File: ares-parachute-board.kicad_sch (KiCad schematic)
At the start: 5 parts, among them J1 Conn_01x16_Female, J2 Conn_01x16_Female, J3 Conn_01x02_Male, U1 STM32F103CBTx

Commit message: rename project
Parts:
- added U2, U3: LIS2DH, Package_LGA:LGA-14_2x2mm_P0.35mm_LayoutBorder3x4y, symbol Sensor_Motion:LIS2DH
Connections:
- new net: U3.10 (GND), U3.11 (GND), U3.12 (GND), U3.13 (GND), U3.14 (GND), U3.9 (GND)
- new net: U2.10 (GND), U2.11 (GND), U2.12 (GND), U2.13 (GND), U2.14 (GND), U2.9 (GND)
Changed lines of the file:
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@@
+	)
+	(symbol
+		(lib_id "Sensor_Motion:LIS2DH")
+		(at 101.6 158.75 0)
+		(unit 1)
+		(exclude_from_sim no)
+		(in_bom yes)
+		(on_board yes)
+		(dnp no)
+		(fields_autoplaced yes)
+		(property "Reference" "U3"
+			(at 103.7941 171.45 0)
+			(effects
+				(font
+					(size 1.27 1.27)
+				)
+				(justify left)
+			)
+		)
+		(property "Value" "LIS2DH"
+			(at 103.7941 173.99 0)
+			(effects
+				(font
+					(size 1.27 1.27)
+				)
+				(justify left)
+			)
+		)
+		(property "Footprint" "Package_LGA:LGA-14_2x2mm_P0.35mm_LayoutBorder3x4y"
+			(at 101.6 170.18 0)
+			(effects
+				(font
+					(size 1.27 1.27)
+				)
+				(hide yes)
+			)
+		)
+		(property "Datasheet" "http://www.st.com/web/en/resource/technical/document/datasheet/DM00042751.pdf"
+			(at 101.6 173.99 0)
+			(effects
+				(font
+					(size 1.27 1.27)
+				)
+				(hide yes)
+			)
+		)
+		(property "Description" "3-Axis Accelerometer, 2/4/8/16g range, I2C/SPI interface, LGA-14"
+			(at 101.6 158.75 0)
+			(effects
+				(font
+					(size 1.27 1.27)
+				)
+				(hide yes)
+			)
+		)
+		(pin "3"
+		)
+		(pin "5"
+		)
+		(pin "12"
+		)
+		(pin "14"
+		)
+		(pin "2"
+		)
+		(pin "13"
+		)
+		(pin "6"
+		)
+		(pin "4"
+		)
+		(pin "11"
+		)
+		(pin "10"
+		)
+		(pin "1"
+		)
+		(pin "9"
+		)
+		(pin "8"
+		)
+		(pin "7"
+		)
+		(instances
+			(project "asyd-parachute"
+				(path "/690fc002-96ff-4ebc-bc23-96072f93f7f5"
+					(reference "U3")
+					(unit 1)
+				)
+			)
+		)
+	)
+	(symbol
+		(lib_id "Sensor_Motion:LIS2DH")
+		(at 71.12 158.75 0)
+		(unit 1)
+		(exclude_from_sim no)
+		(in_bom yes)
+		(on_board yes)
+		(dnp no)
+		(fields_autoplaced yes)
+		(property "Reference" "U2"
+			(at 73.3141 171.45 0)
+			(effects
+				(font
+					(size 1.27 1.27)
+				)
+				(justify left)
+			)
+		)
+		(property "Value" "LIS2DH"
+			(at 73.3141 173.99 0)
+			(effects
+				(font
+					(size 1.27 1.27)
+				)
+				(justify left)
+			)
+		)
+		(property "Footprint" "Package_LGA:LGA-14_2x2mm_P0.35mm_LayoutBorder3x4y"
+			(at 71.12 170.18 0)
+			(effects
+				(font
+					(size 1.27 1.27)
+				)
+				(hide yes)
+			)
+		)
+		(property "Datasheet" "http://www.st.com/web/en/resource/technical/document/datasheet/DM00042751.pdf"
+			(at 71.12 173.99 0)
+			(effects
+				(font
+					(size 1.27 1.27)
+				)
+				(hide yes)
+			)
+		)
+		(property "Description" "3-Axis Accelerometer, 2/4/8/16g range, I2C/SPI interface, LGA-14"
+			(at 71.12 158.75 0)
+			(effects
+				(font
+					(size 1.27 1.27)
+				)
+				(hide yes)
+			)
+		)
+		(pin "3"
+		)
+		(pin "5"
+		)
+		(pin "12"
+		)
+		(pin "14"
+		)
+		(pin "2"
+		)
+		(pin "13"
+		)
+		(pin "6"
+		)
+		(pin "4"
+		)
+		(pin "11"
+		)
+		(pin "10"
+		)
+		(pin "1"
+		)
+		(pin "9"
+		)
+		(pin "8"
+		)
+		(pin "7"
+		)
+		(instances
+			(project ""
+				(path "/690fc002-96ff-4ebc-bc23-96072f93f7f5"
+					(reference "U2")
+					(unit 1)
+				)
+			)
+		)
 	)
 	(symbol

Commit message: update, component selection almost done
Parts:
- removed U2, U3: LIS2DH, Package_LGA:LGA-14_2x2mm_P0.35mm_LayoutBorder3x4y, symbol Sensor_Motion:LIS2DH
- added C1, C2: 20p, Capacitor_SMD:C_0603_1608Metric, symbol Device:C
- added C3, C4: 12.5p, Capacitor_SMD:C_0603_1608Metric, symbol Device:C
- added C5, C6: 47p, Capacitor_SMD:C_0603_1608Metric, symbol Device:C
- added J4: MPT 0.5/2-2.54, TerminalBlock_Phoenix:TerminalBlock_Phoenix_MPT-0,5-2-2.54_1x02_P2.54mm_Horizontal, symbol Connector:Screw_Terminal_01x02
- added J5: Conn_ARM_JTAG_SWD_10, easyeda_exported:IDC-TH_10P-P2.54_C5665, symbol Connector:Conn_ARM_JTAG_SWD_10
- added JP1: Jumper_3_Bridged12, Connector_PinHeader_2.54mm:PinHeader_1x03_P2.54mm_Horizontal, symbol Jumper:Jumper_3_Bridged12
- added LED1, LED4, LED7: RED, easyeda_exported:LED0805-R-RD, symbol easyeda_exported:FC-2012HRK-620D
- added LED2, LED5: YLW, easyeda_exported:LED0805-R-RD, symbol easyeda_exported:17-21SUYC_TR8
- added LED3, LED6: GRN, easyeda_exported:LED0805-R-RD, symbol easyeda_exported:0805G(Green)
- added R1: 0, Resistor_SMD:R_0603_1608Metric, symbol Device:R
- added R2, R3: 5.1k, Resistor_SMD:R_0603_1608Metric, symbol Device:R
- added R4, R5: 33, Resistor_SMD:R_0603_1608Metric, symbol Device:R
- added R6: 100, Resistor_SMD:R_0603_1608Metric, symbol Device:R
- added R7: 56k, Resistor_SMD:R_0603_1608Metric, symbol Device:R
- added R8: 330, Resistor_SMD:R_0603_1608Metric, symbol Device:R
- added U2, U3: LIS2DW12TR, easyeda_exported:LGA-12_L2.0-W2.0-P0.50-BL, symbol easyeda_exported:LIS2DW12TR
- added U4: XC6206P332MR, easyeda_exported:SOT-23-3_L2.9-W1.6-P1.90-LS2.8-BR, symbol easyeda_exported:XC6206P332MR
- added U5: AP2552W6-7, easyeda_exported:SOT-26_L3.0-W1.6-P0.95-LS2.8-BL, symbol easyeda_exported:AP2552W6-7
- added USB1: TYPE-C16PIN, easyeda_exported:USB-C-SMD_TYPE-C16PIN, symbol easyeda_exported:TYPE-C16PIN
- added X1: X49SM8MSD2SC, easyeda_exported:CRYSTAL-SMD_L11.5-W4.8-LS12.7, symbol easyeda_exported:X49SM8MSD2SC
- added X2: Q13FC1350000400, easyeda_exported:FC-135R_L3.2-W1.5, symbol easyeda_exported:Q13FC1350000400
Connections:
- net GND: now also C1.1, C2.1, C3.1, C4.1, C5.2, C6.2, R2.1, R3.1, R6.1, R7.1, U4.1 (GND), U5.2 (GND), U5.3 (~{EN}), USB1.1 (SHELL), USB1.2 (SHELL), USB1.3 (SHELL), USB1.4 (SHELL), USB1.A1B12 (GND), USB1.B1A12 (GND)
- net at U1.3 (PC14): now also C3.2, X2.1
- net at U1.4 (PC15): now also C4.2, X2.2
- net at U1.5 (PD0): now also C1.2, X1.1
- net at U1.6 (PD1): now also R1.2
- net +3V3 renamed +3.3V
- net +3.3V: now also U4.3 (Vout); no longer C1.1
- net MOT-: no longer names the net of J2.3 (Pin_3)
- net MOT-: no longer J1.3 (Pin_3)
- net P0: no longer names the net of J2.4 (Pin_4)
- net P0: no longer J1.4 (Pin_4)
- net P1: no longer names the net of J2.5 (Pin_5)
- net P1: no longer J1.5 (Pin_5)
- net P13: no longer names the net of J2.11 (Pin_11)
- net P13: no longer J1.11 (Pin_11)
- net P14: no longer names the net of J2.12 (Pin_12)
- net P14: no longer J1.12 (Pin_12)
- net P15: no longer names the net of J2.13 (Pin_13)
- net P15: no longer J1.13 (Pin_13)
- net P16: no longer names the net of J2.14 (Pin_14)
- net P16: no longer J1.14 (Pin_14)
- net P19: no longer names the net of J2.15 (Pin_15)
- net P19: no longer J1.15 (Pin_15)
- net P2: no longer names the net of J2.6 (Pin_6)
- net P2: no longer J1.6 (Pin_6)
- net P20: no longer names the net of J2.16 (Pin_16)
- net P20: no longer J1.16 (Pin_16)
- net P8: no longer names the net of J2.9 (Pin_9)
- net P8: no longer J1.9 (Pin_9)
- net P9: no longer names the net of J2.10 (Pin_10)
- net P9: no longer J1.10 (Pin_10)
- net btn_a: no longer names the net of J2.7 (Pin_7)
- net btn_a: no longer J1.7 (Pin_7)
- net btn_b: no longer names the net of J2.8 (Pin_8)
- net btn_b: no longer J1.8 (Pin_8)
- new net: C1.1, JP1.2 (C)
- new net: R8.1, U5.4 (~{FAULT})
- new net: R7.2, U5.5 (ILIM)
- new net: R5.1, USB1.A7 (DN1), USB1.B7 (DN2)
- new net: J5.3 (GND), J5.5 (GND)
- new net: R4.1, USB1.A6 (DP1), USB1.B6 (DP2)
- new net: LED7.2, R8.2
- new net: JP1.3 (B), R6.2
- new net: C2.2, R1.1, X1.2
- new net +5V: JP1.1 (A), U4.2 (Vin), U5.6 (OUT)
- new net VBUS: LED7.1, U5.1 (IN), USB1.A4B9 (VBUS), USB1.B4A9 (VBUS)
- new net cc1: R3.2, USB1.A5 (CC1)
- new net cc2: R2.2, USB1.B5 (CC2)
- new net d+: C5.1, R4.2
- new net d-: C6.1, R5.2
- no-connect marks 2 -> 4
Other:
- note added: "32.768kHz Oscillator"
- note added: "8MHz Oscillator"
- note added: "CBT6"
- note added: "Connector to Detonator"
- note added: "Current Limiter"
- note added: "I_LIM = 19.94/(Rlim/1000)^0.925 -> 481mA"
- note added: "LDO"
- note added: "OSC max: DL_MAX 100-500uW, ESR 60Ohm IqMAX = sqrt(DLmax / ESR) = 2.88mA IqMAX-MCU = 1mA -> Current Limit R_ext not necessary"
- note added: "Supercap disconnect Discharge"
- note added: "TO DO: External Flash"
- note added: "USB-C Plug"
- note added: "Vf ~ 2V"
- moved on the sheet: C1, J1, J2, J3, U1

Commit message: updated schematic
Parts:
- added C10, C11, C13, C14, C18, C8, C9: 100n, Capacitor_SMD:C_0603_1608Metric, symbol Device:C
- added C12: 4u7, Capacitor_SMD:C_0603_1608Metric, symbol Device:C
- added C15, C16: 1u, Capacitor_SMD:C_0603_1608Metric, symbol Device:C
- added C17: 10u, Capacitor_SMD:C_0603_1608Metric, symbol Device:C
- added J6: Conn_01x03_Pin, Connector_PinHeader_2.54mm:PinHeader_1x03_P2.54mm_Horizontal, symbol Connector:Conn_01x03_Pin
- added R10, R11, R12, R9: 4k7, Resistor_SMD:R_0603_1608Metric, symbol Device:R
- added U6: W25Q128JVSIQTR, easyeda_exported:SOIC-8_L5.3-W5.3-P1.27-LS8.0-BL, symbol easyeda_exported:W25Q128JVSIQTR
- added U7: SR05-ES, Package_TO_SOT_SMD:SOT-143, symbol easyeda_exported:SR05-ES
- J4: renamed from J5; footprint easyeda_exported:IDC-TH_10P-P2.54_C5665 -> Connector_PinHeader_1.27mm:PinHeader_2x05_P1.27mm_Vertical; LCSC Part (none) -> C7501289
- renumbered C5 to C1, C6 to C2, C1 to C3, C2 to C4, C3 to C5, C4 to C6, C1 to C7, J4 to J5, LED7 to LED1, LED1 to LED2, LED2 to LED3, LED3 to LED4, LED4 to LED5, LED5 to LED6, LED6 to LED7, R4 to R1, R8 to R2, R5 to R3, R7 to R4, R3 to R5, R2 to R6, R1 to R7, R6 to R8, U4 to U1, U5 to U2, U2 to U3, U1 to U4, U3 to U5
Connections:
- net +3.3V: now also J4.1 (VTref), U3.10 (VDDIO), U3.2 (CS), U3.9 (VDD), U4.24 (VDD), U4.36 (VDD), U4.48 (VDD), U4.9 (VDDA), U5.10 (VDDIO), U5.2 (CS), U5.9 (VDD), C10.1, C11.1, C12.1, C13.1, C14.1, C16.1, C8.1, C9.1, R10.2, R11.1, R12.2, R9.1
- net +5V: now also C15.1
- net GND: now also J4.3 (GND), J4.5 (GND), J4.9 (GNDDetect), U3.3 (SDO/SA0), U3.6 (GND), U3.7 (RES), U3.8 (GND), U4.23 (VSS), U4.35 (VSS), U4.47 (VSS), U4.8 (VSSA), U5.3 (SDO/SA0), U5.6 (GND), U5.7 (RES), U5.8 (GND), C10.2, C11.2, C12.2, C13.2, C14.2, C15.2, C16.2, C17.2, C18.2, C8.2, C9.2, J6.3 (Pin_3), U7.1 (GND)
- net VBUS: now also C17.1, C18.1, U7.4 (VCC)
- net at R3.1, USB1.A7 (DN1), USB1.B7 (DN2): now also U7.2 (IO)
- net ~{RESET}: now reaches J4.10 (~{RESET})
- net ~{RESET}: now also U4.7 (NRST)
- net SWDIO: now reaches J4.2 (SWDIO/TMS)
- net SWDIO: now also U4.34 (PA13)
- net SWCLK: now reaches J4.4 (SWCLK/TCK)
- net SWCLK: now also U4.37 (PA14)
- net SWO: now reaches J4.6 (SWO/TDO)
- net SWO: now also U4.39 (PB3)
- net at R1.1, USB1.A6 (DP1), USB1.B6 (DP2): now also U7.3 (IO)
- net I2C2_SCL: now reaches U5.1 (SCL/SPC)
- net I2C2_SCL: now also U4.21 (PB10), R9.2
- net I2C2_SDA: now reaches U5.4 (SDA/SDI/SDO)
- net I2C2_SDA: now also U4.22 (PB11), R10.1
- net SPI1_SCK: now reaches U4.15 (PA5)
- net SPI1_MISO: now reaches U4.16 (PA6)
- net SPI1_MOSI: now reaches U4.17 (PA7)
- net USART1_TX: now reaches U4.30 (PA9)
- net USART1_TX: now also J6.1 (Pin_1)
- net USART1_RX: now reaches U4.31 (PA10)
- net USART1_RX: now also J6.2 (Pin_2)
- net I2C1_SCL: now reaches U4.42 (PB6)
- net I2C1_SCL: now also U3.1 (SCL/SPC), R11.2
- net I2C1_SDA: now reaches U4.43 (PB7)
- net I2C1_SDA: now also U3.4 (SDA/SDI/SDO), R12.1
- no-connect marks 4 -> 11
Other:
- note added: "Decoupling MCU"
- note added: "NOR Flash"
- note added: "TO DO: External Flash Stützkondis"
- note added: "TVS"
- note removed: "TO DO: External Flash"
- moved on the sheet: C1, C2, C3, C4, C5, C6, C7, J3, J4, J5, JP1, R1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

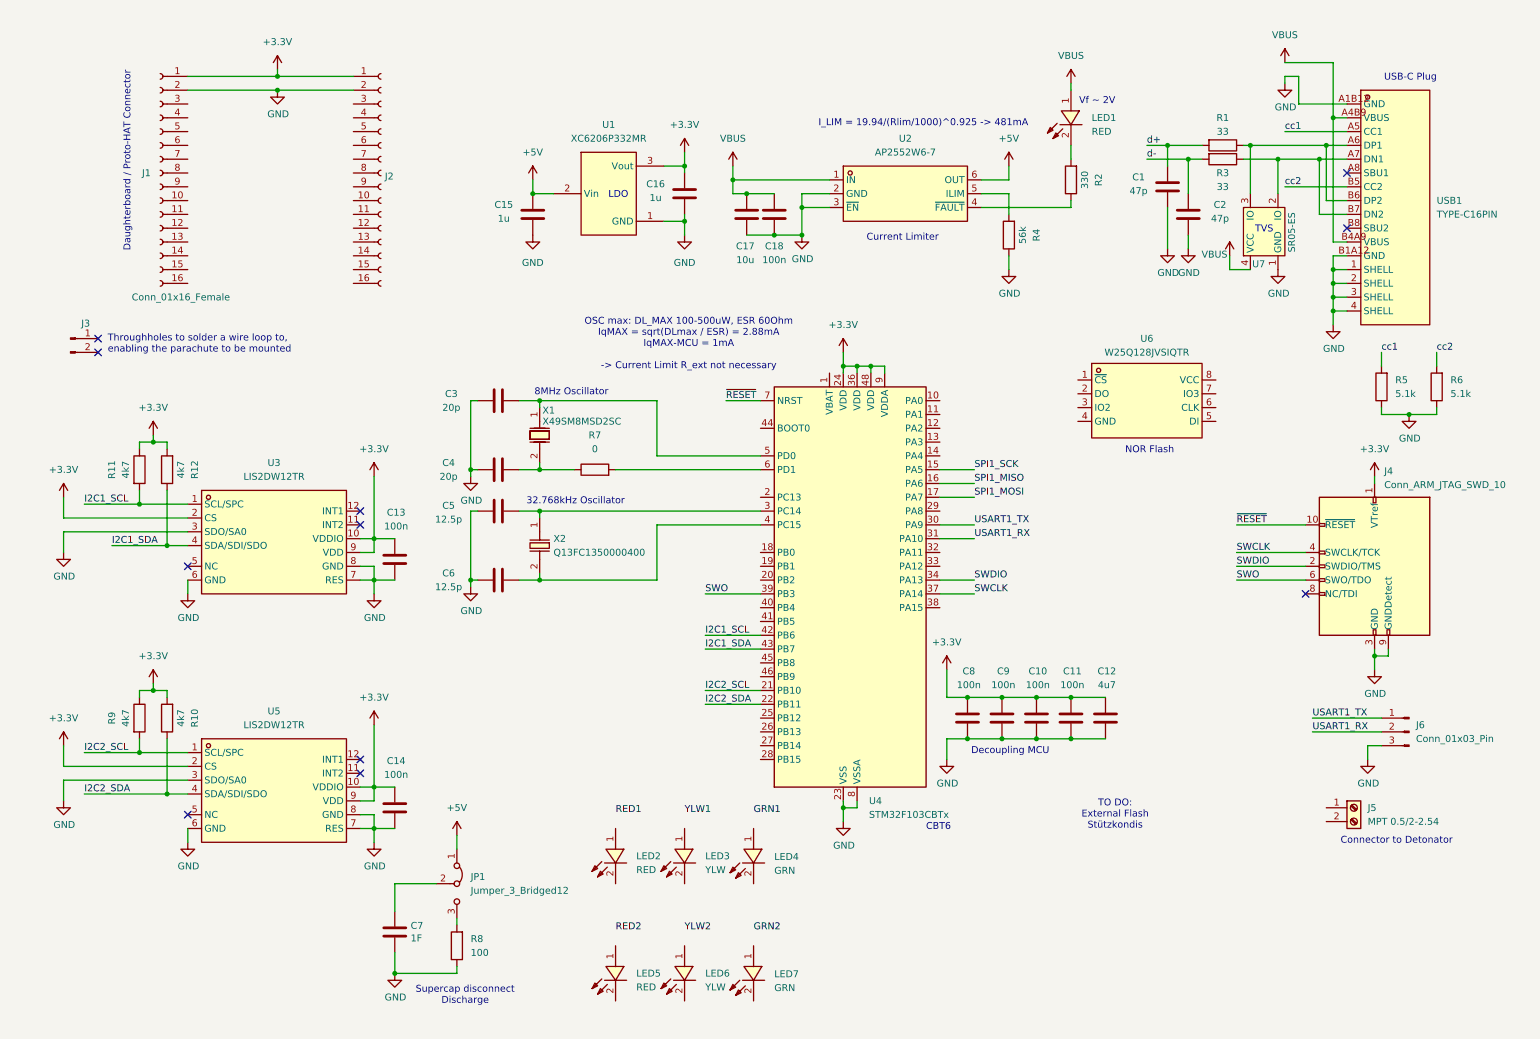
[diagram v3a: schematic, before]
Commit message: updated schematic, moving on to routing
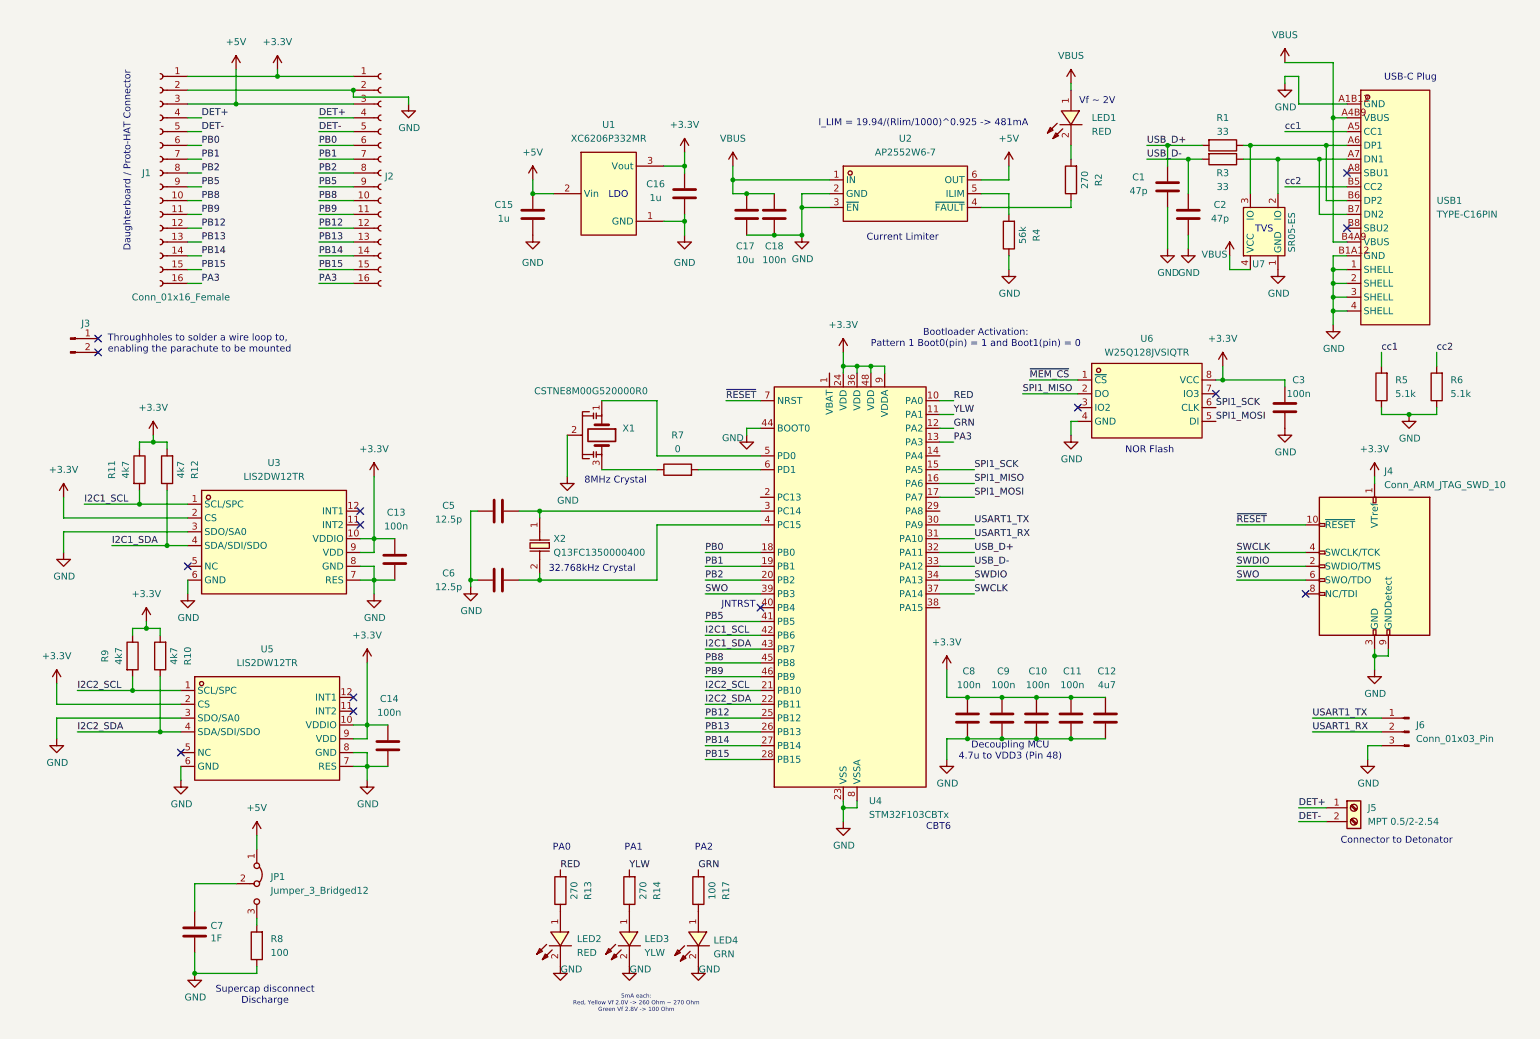
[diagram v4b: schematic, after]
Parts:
- removed C4: 20p, Capacitor_SMD:C_0603_1608Metric, symbol Device:C
- removed LED5: RED, easyeda_exported:LED0805-R-RD, symbol easyeda_exported:FC-2012HRK-620D
- removed LED6: YLW, easyeda_exported:LED0805-R-RD, symbol easyeda_exported:17-21SUYC_TR8
- removed LED7: GRN, easyeda_exported:LED0805-R-RD, symbol easyeda_exported:0805G(Green)
- removed X1: X49SM8MSD2SC, easyeda_exported:CRYSTAL-SMD_L11.5-W4.8-LS12.7, symbol easyeda_exported:X49SM8MSD2SC
- added R13, R14: 270, Resistor_SMD:R_0603_1608Metric, symbol Device:R
- added R17: 100, Resistor_SMD:R_0603_1608Metric, symbol Device:R
- added X1: CSTNE8M00G520000R0, easyeda_exported:OSC-SMD_3P-L3.2-W1.3-P1.20, symbol easyeda_exported:CSTNE8M00G520000R0
- C3: value 20p -> 100n
- R2: value 330 -> 270
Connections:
- net d+ is gone; now on net USB_D+: C1.1, R1.2
- net d- is gone; now on net USB_D-: C2.1, R3.2
- net +3.3V: now also C3.1, U6.8 (VCC)
- net +5V: now also J1.3 (Pin_3), J2.3 (Pin_3)
- net GND: now also C3.2, LED2.2, LED3.2, LED4.2, U4.44 (BOOT0), U6.4 (GND), X1.2; no longer C3.1
- net SPI1_MISO: now also U6.2 (DO)
- net SPI1_MOSI: now also U6.5 (DI)
- net SPI1_SCK: now also U6.6 (CLK)
- net PB8: now reaches J2.10 (Pin_10)
- net PB8: now also J1.10 (Pin_10), U4.45 (PB8)
- net PB9: now reaches J2.11 (Pin_11)
- net PB9: now also J1.11 (Pin_11), U4.46 (PB9)
- net PB12: now reaches J2.12 (Pin_12)
- net PB12: now also J1.12 (Pin_12), U4.25 (PB12)
- net PB13: now reaches J2.13 (Pin_13)
- net PB13: now also J1.13 (Pin_13), U4.26 (PB13)
- net PB14: now reaches J2.14 (Pin_14)
- net PB14: now also J1.14 (Pin_14), U4.27 (PB14)
- net PB15: now reaches J2.15 (Pin_15)
- net PB15: now also J1.15 (Pin_15), U4.28 (PB15)
- net PA3: now reaches J2.16 (Pin_16)
- net PA3: now also J1.16 (Pin_16), U4.13 (PA3)
- net DET+: now reaches J2.4 (Pin_4)
- net DET+: now also J1.4 (Pin_4), J5.1 (Pin_1)
- net DET-: now reaches J2.5 (Pin_5)
- net DET-: now also J1.5 (Pin_5), J5.2 (Pin_2)
- net PB0: now reaches J2.6 (Pin_6)
- net PB0: now also J1.6 (Pin_6), U4.18 (PB0)
- net PB1: now reaches J2.7 (Pin_7)
- net PB1: now also J1.7 (Pin_7), U4.19 (PB1)
- net PB2: now reaches J2.8 (Pin_8)
- net PB2: now also J1.8 (Pin_8), U4.20 (PB2)
- net PB5: now reaches J2.9 (Pin_9)
- net PB5: now also J1.9 (Pin_9), U4.41 (PB5)
- net at U4.5 (PD0): now also X1.1; no longer C3.2
- net at LED2.1: now also R13.1
- net at LED3.1: now also R14.1
- net at R7.1: now also X1.3
- net at LED4.1: now also R17.1
- net RED: now reaches U4.10 (PA0)
- net RED: now also R13.2
- net YLW: now reaches U4.11 (PA1)
- net YLW: now also R14.2
- net GRN: now reaches U4.12 (PA2)
- net GRN: now also R17.2
- net USB_D+: now reaches U4.32 (PA11)
- net USB_D-: now reaches U4.33 (PA12)
- net ~{MEM_CS}: now reaches U6.1 (~{CS})
- no-connect marks 11 -> 14
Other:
- note added: "32.768kHz Crystal"
- note added: "5mA each: Red, Yellow Vf 2.0V -> 260 Ohm ~ 270 Ohm Green Vf 2.8V -> 100 Ohm"
- note added: "8MHz Crystal"
- note added: "Bootloader Activation: Pattern 1 Boot0(pin) = 1 and Boot1(pin) = 0"
- note added: "Decoupling MCU 4.7u to VDD3 (Pin 48)"
- note added: "JNTRST"
- note added: "PA0"
- note added: "PA1"
- note added: "PA2"
- note removed: "32.768kHz Oscillator"
- note removed: "8MHz Oscillator"
- note removed: "Decoupling MCU"
- note removed: "OSC max: DL_MAX 100-500uW, ESR 60Ohm IqMAX = sqrt(DLmax / ESR) = 2.88mA IqMAX-MCU = 1mA -> Current Limit R_ext not necessary"
- note removed: "TO DO: External Flash Stützkondis"
- company: (none) -> Hochschule Luzern, Technik & Architektur
- title: (none) -> ARES Parachute Board
- moved on the sheet: C14, C7, JP1, LED2, LED3, LED4, R10, R7, R8, R9, U5

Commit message: re-annotate, component placement complete
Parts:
- renumbered C6 to C10, C8 to C11, C9 to C12, C10 to C13, C11 to C14, C12 to C15, C14 to C16, C7 to C17, C16 to C2, C15 to C3, C17 to C4, C18 to C5, C2 to C6, C3 to C7, C5 to C8, C13 to C9, J6 to J5, J5 to J6, R9 to R10, R10 to R11, R13 to R12, R14 to R13, R17 to R14, R8 to R15, R3 to R2, R2 to R3, R11 to R7, R12 to R8, R7 to R9, U7 to U3, U6 to U4, U3 to U5, U4 to U6, U5 to U7

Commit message: about to try some stuff
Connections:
- net +3.3V: no longer J2.1 (Pin_1)
- net +5V: no longer J2.3 (Pin_3)
- net DET+: no longer J2.4 (Pin_4)
- net DET-: no longer J2.5 (Pin_5)
- net GND: no longer J2.2 (Pin_2)
- net PA3: no longer J2.16 (Pin_16)
- net PB0: no longer J2.6 (Pin_6)
- net PB1: no longer J2.7 (Pin_7)
- net PB12: no longer J2.12 (Pin_12)
- net PB13: no longer J2.13 (Pin_13)
- net PB14: no longer J2.14 (Pin_14)
- net PB15: no longer J2.15 (Pin_15)
- net PB2: no longer J2.8 (Pin_8)
- net PB5: no longer J2.9 (Pin_9)
- net PB8: no longer J2.10 (Pin_10)
- net PB9: no longer J2.11 (Pin_11)
- net USART1_RX: now also J5.1 (Pin_1); no longer J5.2 (Pin_2)
- net USART1_TX: now also J5.2 (Pin_2); no longer J5.1 (Pin_1)
- net d-: now reaches R2.1, U3.2 (IO), USB1.A7 (DN1), USB1.B7 (DN2)
- net d+: now reaches R1.1, U3.3 (IO), USB1.A6 (DP1), USB1.B6 (DP2)
- no-connect marks 14 -> 27
